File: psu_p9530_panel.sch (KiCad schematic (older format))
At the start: 56 parts, among them IC306 LTC1658, IC308 CD4052B, IC310 TLC272, IC312 TLC272, U401 74HCT164

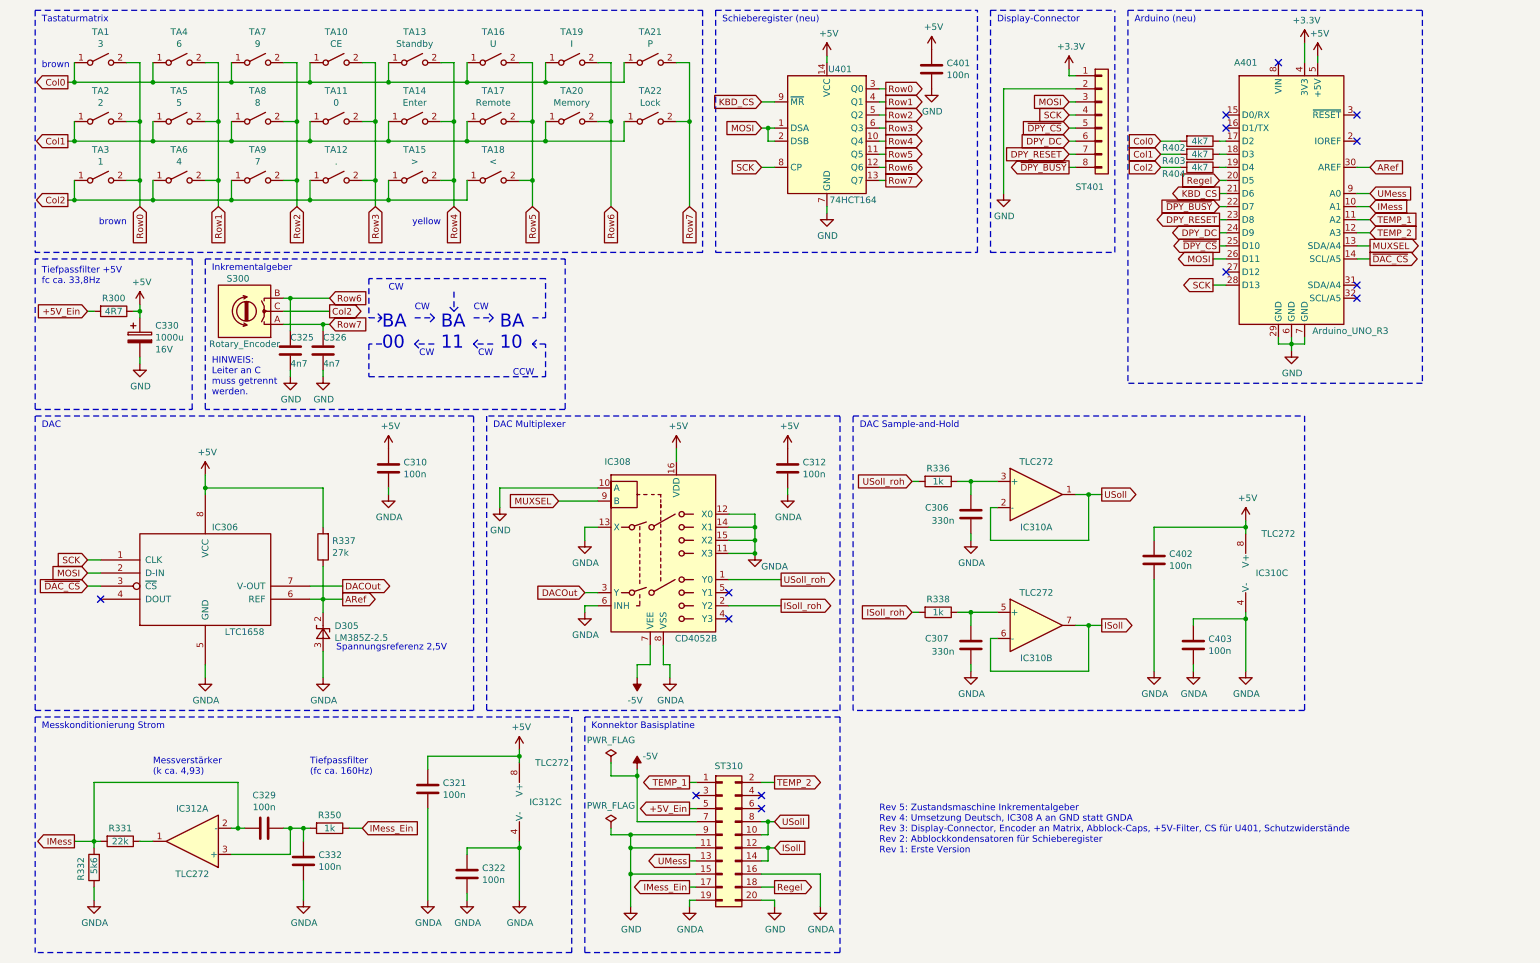
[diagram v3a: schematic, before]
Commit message: Fix schematic errors, fix handling of incremental encoder
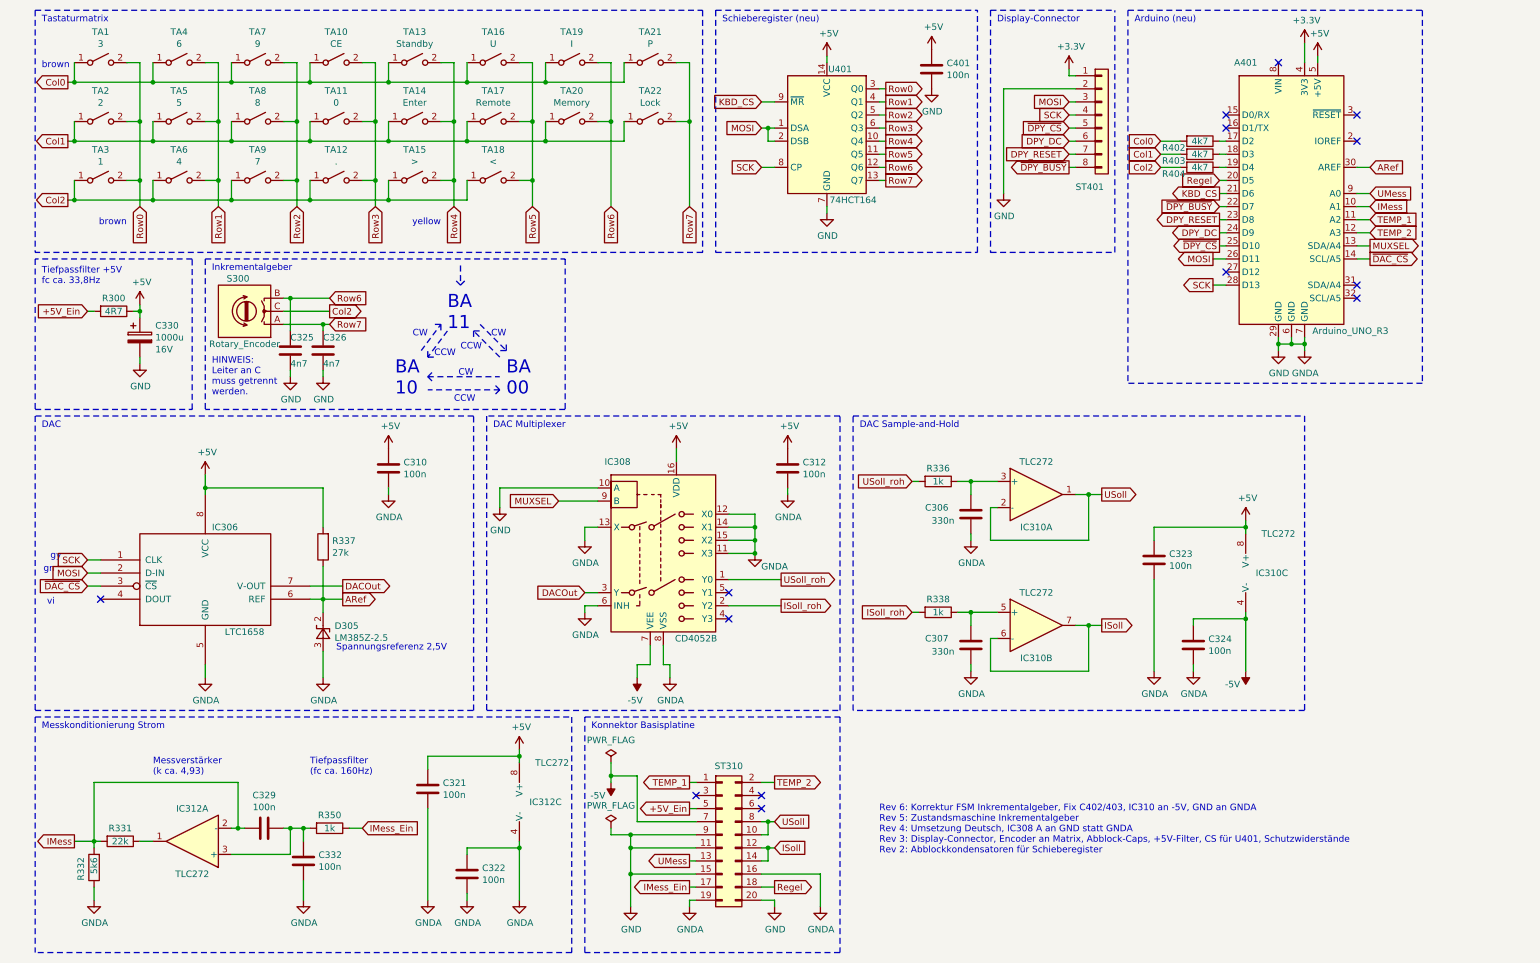
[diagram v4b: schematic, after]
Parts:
- renumbered C402 to C323, C403 to C324
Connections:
- net -5V: now also C324.1, IC310.4 (V-)
- net GND: now also C306.2, C307.2, C310.2, C312.2, C321.2, C322.1, C322.2, C323.2, C324.2, C332.2, D305.3 (A), IC306.5 (GND), IC308.11 (X3), IC308.12 (X0), IC308.13 (X), IC308.14 (X1), IC308.15 (X2), IC308.6 (INH), IC308.8 (VSS), IC312.4 (V-), R332.1, ST310.16 (Pin_16), ST310.19 (Pin_19)
- removed net GNDA: C306.2, C307.2, C310.2, C312.2, C321.2, C322.1, C322.2, C323.2, C324.1, C324.2, C332.2, D305.3 (A), IC306.5 (GND), IC308.11 (X3), IC308.12 (X0), IC308.13 (X), IC308.14 (X1), IC308.15 (X2), IC308.6 (INH), IC308.8 (VSS), IC310.4 (V-), IC312.4 (V-), R332.1, ST310.16 (Pin_16), ST310.19 (Pin_19)
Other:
- note added: "Rev 6: Korrektur FSM Inkrementalgeber, Fix C402/403, IC310 an -5V, GND an GNDA\nRev 5: Zustandsmaschine Inkrementalgeber\nRev 4: Umsetzung Deutsch, IC308 A an GND statt GNDA\nRev 3: Display-Connector, Encoder an Matrix, Abblock-Caps, +5V-Filter, CS für U401, Schutzwiderstände\nRev 2: Abblockkondensatoren für Schieberegister"
- note added: "gn"
- note added: "gy"
- note added: "vi"
- note removed: "Rev 5: Zustandsmaschine Inkrementalgeber\nRev 4: Umsetzung Deutsch, IC308 A an GND statt GNDA\nRev 3: Display-Connector, Encoder an Matrix, Abblock-Caps, +5V-Filter, CS für U401, Schutzwiderstände\nRev 2: Abblockkondensatoren für Schieberegister\nRev 1: Erste Version"
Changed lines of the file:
@@
 Sheet 1 1
 Title "ELV PS9530 Ersatz Bedienteil"
-Date "2022-08-12"
-Rev "5"
+Date "2022-08-20"
+Rev "6"
 Comp "Ralf Gerlich"
 Comment1 ""
@@
 L power:-5V #PWR0101
 U 1 1 62ED6C70
-P 5150 6350
-F 0 "#PWR0101" H 5150 6450 50  0001 C CNN
-F 1 "-5V" H 5250 6450 50  0000 C CNN
-F 2 "" H 5150 6350 50  0001 C CNN
-F 3 "" H 5150 6350 50  0001 C CNN
-	1    5150 6350
-	1    0    0    -1
+P 4950 6450
+F 0 "#PWR0101" H 4950 6550 50  0001 C CNN
+F 1 "-5V" H 5050 6550 50  0000 C CNN
+F 2 "" H 4950 6450 50  0001 C CNN
+F 3 "" H 4950 6450 50  0001 C CNN
+	1    4950 6450
+	-1   0    0    1
 $EndComp
 $Comp
@@
 L power:GND #PWR0125
 U 1 1 6343CDB8
-P 10150 3150
-F 0 "#PWR0125" H 10150 2900 50  0001 C CNN
-F 1 "GND" H 10155 2977 50  0000 C CNN
-F 2 "" H 10150 3150 50  0001 C CNN
-F 3 "" H 10150 3150 50  0001 C CNN
-	1    10150 3150
+P 10050 3150
+F 0 "#PWR0125" H 10050 2900 50  0001 C CNN
+F 1 "GND" H 10055 2977 50  0000 C CNN
+F 2 "" H 10050 3150 50  0001 C CNN
+F 3 "" H 10050 3150 50  0001 C CNN
+	1    10050 3150
 	1    0    0    -1
 $EndComp
@@
 Wire Wire Line
 	10050 3100 10150 3100
-Wire Wire Line
-	10150 3100 10150 3150
 Wire Wire Line
 	10150 3050 10150 3100
@@
 $EndComp
 $Comp
-L Device:C C402
+L Device:C C323
 U 1 1 63524055
 P 9100 4750
-F 0 "C402" H 9215 4796 50  0000 L CNN
+F 0 "C323" H 9215 4796 50  0000 L CNN
 F 1 "100n" H 9215 4705 50  0000 L CNN
 F 2 "" H 9138 4600 50  0001 C CNN
@@
 $EndComp
 $Comp
-L Device:C C403
+L Device:C C324
 U 1 1 6352405B
 P 9400 5400
-F 0 "C403" H 9515 5446 50  0000 L CNN
+F 0 "C324" H 9515 5446 50  0000 L CNN
 F 1 "100n" H 9515 5355 50  0000 L CNN
 F 2 "" H 9438 5250 50  0001 C CNN
 F 3 "~" H 9400 5400 50  0001 C CNN
 	1    9400 5400
-	1    0    0    -1
-$EndComp
-$Comp
-L power:GNDA #PWR0414
-U 1 1 63524061
-P 9800 5600
-F 0 "#PWR0414" H 9800 5350 50  0001 C CNN
-F 1 "GNDA" H 9805 5427 50  0000 C CNN
-F 2 "" H 9800 5600 50  0001 C CNN
-F 3 "" H 9800 5600 50  0001 C CNN
-	1    9800 5600
 	1    0    0    -1
 $EndComp
@@
 	1750 3600 1750 2450
 Text Notes 7000 7000 0    50   ~ 0
-Rev 5: Zustandsmaschine Inkrementalgeber\nRev 4: Umsetzung Deutsch, IC308 A an GND statt GNDA\nRev 3: Display-Connector, Encoder an Matrix, Abblock-Caps, +5V-Filter, CS für U401, Schutzwiderstände\nRev 2: Abblockkondensatoren für Schieberegister\nRev 1: Erste Version
+Rev 6: Korrektur FSM Inkrementalgeber, Fix C402/403, IC310 an -5V, GND an GNDA\nRev 5: Zustandsmaschine Inkrementalgeber\nRev 4: Umsetzung Deutsch, IC308 A an GND statt GNDA\nRev 3: Display-Connector, Encoder an Matrix, Abblock-Caps, +5V-Filter, CS für U401, Schutzwiderstände\nRev 2: Abblockkondensatoren für Schieberegister
 $Comp
 L Device:R R402
@@
 $EndComp
 Wire Wire Line
-	5150 6350 5150 6400
-Wire Wire Line
 	4950 6300 4950 6400
 Wire Wire Line
 	4950 6400 5150 6400
-Connection ~ 5150 6400
 Wire Wire Line
 	5150 6400 5150 6750
@@
 Text Notes 600  1000 0    50   ~ 0
 brown
-Text Notes 3200 3150 0    100  ~ 0
+Text Notes 4150 3500 0    100  ~ 0
 BA\n00
-Text Notes 4100 3150 0    100  ~ 0
+Text Notes 3300 3500 0    100  ~ 0
 BA\n10
+Text Notes 3800 3150 0    50   ~ 0
+CCW
+Wire Notes Line
+	1850 2450 4600 2450
+Wire Notes Line
+	4600 2450 4600 3600
+Wire Notes Line
+	4600 3600 1850 3600
+Text Notes 3700 3000 0    100  ~ 0
+BA\n11
 Wire Notes Line style solid
-	3450 2900 3600 2900
+	3550 3350 3600 3400
 Wire Notes Line style solid
-	3600 2900 3550 2850
-Wire Notes Line style solid
-	3600 2900 3550 2950
-Text Notes 3450 2850 0    50   ~ 0
+	3550 3350 3600 3300
+Text Notes 4150 3050 2    50   ~ 0
 CW
 Wire Notes Line style solid
-	4350 2900 4450 2900
+	3800 2500 3800 2650
 Wire Notes Line style solid
-	4450 2900 4450 2600
+	3800 2650 3850 2600
 Wire Notes Line style solid
-	4450 2600 3100 2600
+	3800 2650 3750 2600
 Wire Notes Line style solid
-	3100 2600 3100 2900
+	3950 2950 4150 3150
 Wire Notes Line style solid
-	3100 2900 3200 2900
+	4150 3150 4150 3100
 Wire Notes Line style solid
-	3200 2900 3150 2850
+	4150 3150 4100 3150
 Wire Notes Line style solid
-	3200 2900 3150 2950
-Wire Notes Line style solid
-	3200 3100 3100 3100
-Wire Notes Line style solid
-	3100 3100 3100 3350
-Wire Notes Line style solid
-	3100 3350 4450 3350
-Wire Notes Line style solid
-	4450 3350 4450 3100
-Wire Notes Line style solid
-	4450 3100 4350 3100
-Wire Notes Line style solid
-	4350 3100 4400 3050
-Wire Notes Line style solid
-	4350 3100 4400 3150
-Text Notes 3250 2700 0    50   ~ 0
-CW
-Text Notes 4200 3350 0    50   ~ 0
-CCW
-Wire Notes Line
-	1850 2450 4600 2450
-Wire Notes Line
-	4600 2450 4600 3600
-Wire Notes Line
-	4600 3600 1850 3600
-Wire Notes Line style solid
-	3900 2900 4050 2900
-Wire Notes Line style solid
-	4050 2900 4000 2850
-Wire Notes Line style solid
-	4050 2900 4000 2950
-Text Notes 3900 2850 0    50   ~ 0
-CW
-Text Notes 3650 3150 0    100  ~ 0
-BA\n11
-Wire Notes Line style solid
-	3600 3100 3450 3100
-Wire Notes Line style solid
-	3450 3100 3500 3150
-Wire Notes Line style solid
-	3450 3100 3500 3050
-Text Notes 3600 3200 2    50   ~ 0
+	3550 3350 4100 3350
+Text Notes 3900 3350 2    50   ~ 0
 CW
 Wire Notes Line style solid
-	4050 3100 3900 3100
+	3500 3150 3650 2950
 Wire Notes Line style solid
-	3900 3100 3950 3150
+	3650 2950 3600 2950
 Wire Notes Line style solid
-	3900 3100 3950 3050
-Text Notes 4050 3200 2    50   ~ 0
+	3650 2950 3650 3000
+Text Notes 3550 3050 2    50   ~ 0
 CW
 Wire Notes Line style solid
-	3750 2700 3750 2850
+	4100 3200 3900 3000
 Wire Notes Line style solid
-	3750 2850 3800 2800
+	3900 3000 3900 3050
 Wire Notes Line style solid
-	3750 2850 3700 2800
+	3900 3000 3950 3000
+Wire Notes Line style solid
+	4100 3450 4050 3400
+Wire Notes Line style solid
+	4100 3450 4050 3500
+Wire Notes Line style solid
+	4100 3450 3550 3450
+Text Notes 3750 3550 0    50   ~ 0
+CCW
+Wire Notes Line style solid
+	3700 3000 3550 3200
+Wire Notes Line style solid
+	3550 3200 3600 3200
+Wire Notes Line style solid
+	3550 3200 3550 3150
+Text Notes 3600 3200 0    50   ~ 0
+CCW
+$Comp
+L power:-5V #PWR?
+U 1 1 631DA4D4
+P 9800 5600
+F 0 "#PWR?" H 9800 5700 50  0001 C CNN
+F 1 "-5V" H 9900 5700 50  0000 C CNN
+F 2 "" H 9800 5600 50  0001 C CNN
+F 3 "" H 9800 5600 50  0001 C CNN
+	1    9800 5600
+	-1   0    0    1
+$EndComp
+Wire Wire Line
+	4950 6400 4950 6450
+Connection ~ 4950 6400
+Wire Wire Line
+	10050 3100 10050 3150
+Connection ~ 10050 3100
+$Comp
+L power:GNDA #PWR?
+U 1 1 6320F424
+P 10250 3150
+F 0 "#PWR?" H 10250 2900 50  0001 C CNN
+F 1 "GNDA" H 10255 2977 50  0000 C CNN
+F 2 "" H 10250 3150 50  0001 C CNN
+F 3 "" H 10250 3150 50  0001 C CNN
+	1    10250 3150
+	1    0    0    -1
+$EndComp
+Wire Wire Line
+	10250 3150 10250 3100
+Connection ~ 10250 3100
+Text Notes 750  4750 2    50   ~ 0
+gy
+Text Notes 700  4850 2    50   ~ 0
+gn
+Text Notes 700  5100 2    50   ~ 0
+vi
 $EndSCHEMATC
